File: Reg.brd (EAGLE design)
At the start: 30.5 x 21 mm, 28 parts, among them Q1 NPN2SC3422-2, Q2 NPN2SC3325, Q3 PNP2SA1313, Q4 NPN2SC3325, Q5 NPN2SC3422-2, Q6 NPN2SC3325, Q7 PNP2SA1313, Q8 PNP2SA1313

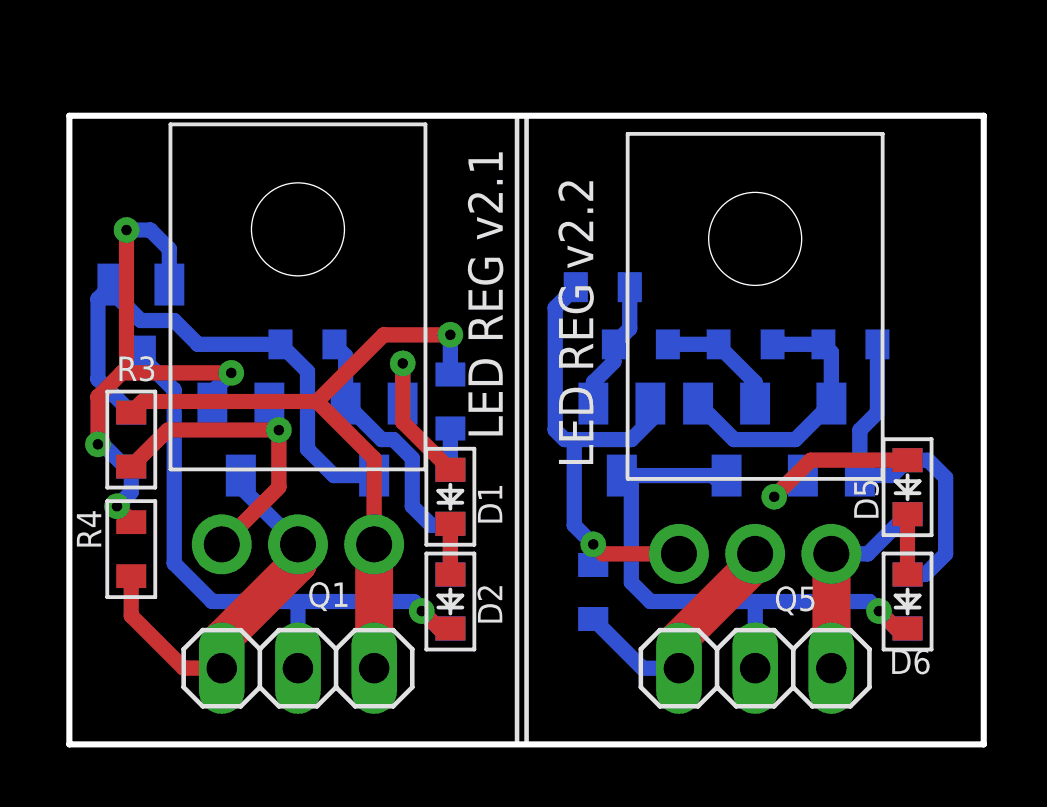
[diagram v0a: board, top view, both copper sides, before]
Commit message: 幅を小さくした
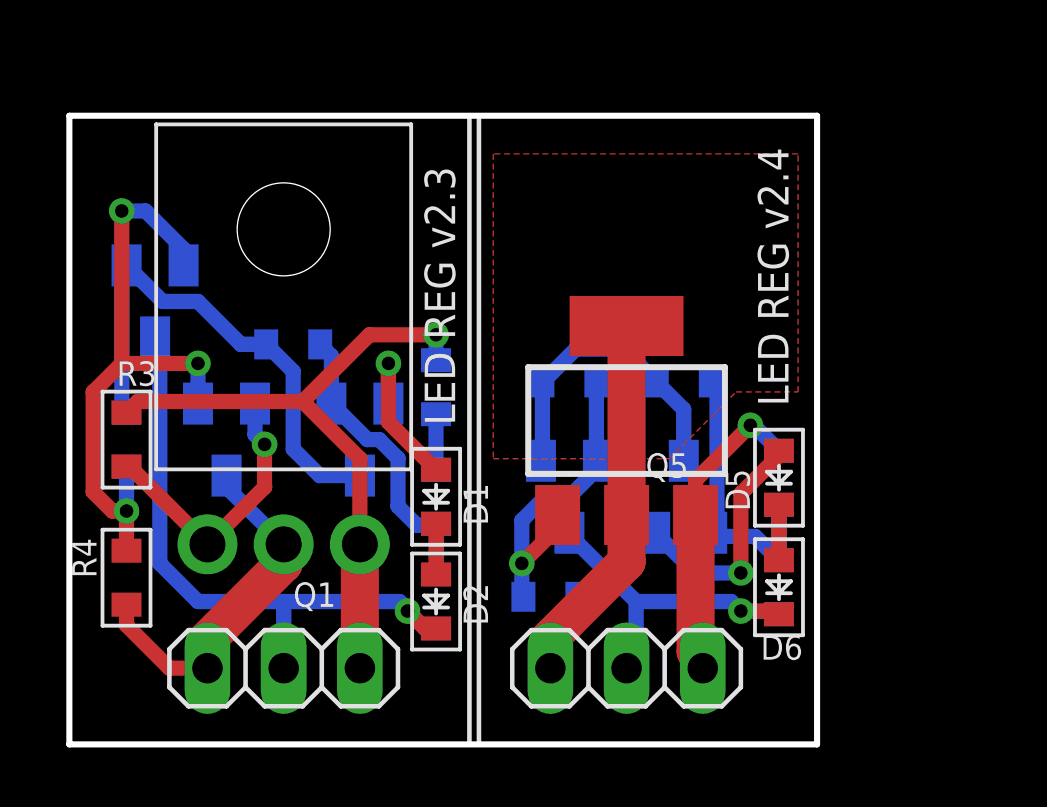
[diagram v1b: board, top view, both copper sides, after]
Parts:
- removed D3, D4: BLUE, my_rcl:D1608
- removed Q7: PNP2SA1313, my_ic:SC59
- D1, D2: value SHORT -> BLUE
- Q1: value NPN2SC3422-2 -> NPN
- Q2, Q4, Q6: value NPN2SC3325 -> NPN
- Q3, Q8: value PNP2SA1313 -> PNP
- Q5: value NPN2SC3422-2 -> NPN; device my_ic:TO126-2 -> my_ic:SOT223
- R10: value 0.75k -> 1.5k
- moved R6 11.5 mm to (12.2, 8.26), turned to 90 degrees
- moved R7 6.97 mm to (12.2, 11.9), turned to 90 degrees
- moved Q5 6.17 mm to (18.6, 10.8)
- moved C1 5.70 mm to (20.5, 12.1)
- moved Q6 5.28 mm to (20.5, 8.26)
- moved D6 4.31 mm to (23.7, 5.24)
- moved R5 4.31 mm to (23.7, 5.24)
- moved D5 4.30 mm to (23.7, 8.89)
- moved R12 4.30 mm to (23.7, 8.89), turned to 90 degrees
- moved JP2 4.29 mm to (18.6, 2.54)
- moved R10 3.36 mm to (16.7, 12.1), turned to 180 degrees
- moved Q8 2.58 mm to (16.7, 8.26)
- moved R9 1.44 mm to (16.0, 4.92), turned to 180 degrees
- moved R4 0.97 mm to (1.91, 5.56)
- moved Q3 0.79 mm to (2.86, 14.8)
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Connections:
- removed net N$11: Q7.2, R6.2, R7.1
- removed net N$15: Q8.1, R10.1, R7.2
- net GND1: no longer Q7.3
- net IN1: now also Q5.4
- net N$12: now also Q8.1, R10.1; no longer Q7.1, R6.1
- net N$16: now also Q5.1; no longer Q5.3
- net N$3: now also R6.1; no longer D3.K
- net N$5: now also R6.2, R7.1; no longer D3.A, D4.K
- net OUT: now also R7.2; no longer D4.A
- net OUT1: now also Q5.3; no longer Q5.1
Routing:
- net GND1: track 20.6 -> 11.8 mm
- net IN1: track 8.40 -> 15.2 mm
- net N$16: track 16.6 -> 10.8 mm
- net N$15: track 4.38 -> 0.00 mm
- net N$11: track 4.17 -> 0.00 mm
- net OUT1: track 6.90 -> 10.3 mm, vias 0 -> 1
- net N$13: track 12.0 -> 9.62 mm
- net N$1: track 19.1 -> 21.0 mm, vias 4 -> 3
- net N$9: track 6.20 -> 8.01 mm
- net N$6: track 11.0 -> 9.39 mm
- net N$12: track 9.21 -> 10.3 mm
- net IN: track 13.3 -> 12.2 mm
- net OUT: track 22.7 -> 21.9 mm
- net N$10: track 18.0 -> 17.2 mm
- added copper zone on layer 1, net IN1
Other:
- board size 30.5 x 21 mm -> 24.9 x 21 mm
- board text added: "LED REG v2.3"
- board text added: "LED REG v2.4"
- board text removed: "LED REG v2.1"
- board text removed: "LED REG v2.2"

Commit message: V-CUT
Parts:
- added C10, C11, C12, C13, C14, C15, C16, C17, C18, C2, C3, C4, C5, C6, C8, C9: 100p, my_rcl:1608
- added D10, D11, D12, D13, D14, D15, D16, D17, D18, D19, D20, D21, D22, D23, D24, D25, D26, D27, D28, D29, D3, D30, D31, D32, D33, D34, D35, D36, D4, D7, D8, D9: BLUE, my_rcl:D1608
- added JP10, JP11, JP12, JP13, JP14, JP15, JP16, JP17, JP18, JP3, JP4, JP5, JP6, JP7, JP8, JP9: CON, pinhead:1X03
- added Q10, Q14, Q17, Q21, Q24, Q28, Q31, Q35, Q38, Q42, Q45, Q49, Q52, Q56, Q59, Q63: PNP, my_ic:SC59
- added Q11, Q13, Q16, Q18, Q20, Q23, Q25, Q27, Q30, Q32, Q34, Q37, Q39, Q41, Q44, Q46, Q48, Q51, Q53, Q55, Q58, Q60, Q62, Q9: NPN, my_ic:SC59
- added Q12, Q19, Q26, Q33, Q40, Q47, Q54, Q61: NPN, my_ic:SOT223
- added Q15, Q22, Q29, Q36, Q43, Q50, Q57, Q7: NPN, my_ic:TO126-2
- added R11, R13, R15, R16, R17, R18, R19, R20, R21, R22, R23, R25, R26, R27, R28, R29, R30, R31, R32, R33, R35, R36, R37, R38, R39, R40, R41, R42, R43, R45, R46, R47, R48, R49, R50, R51, R52, R53, R55, R56, R57, R58, R59, R60, R61, R62, R63, R65, R66, R67, R68, R69, R70, R71, R72, R73, R75, R76, R77, R78, R79, R8, R80, R81, R82, R83, R85, R86, R87, R88, R89, R90: 1.5k, my_rcl:1608
- added R14, R24, R34, R44, R54, R64, R74, R84: 10k, my_rcl:1608
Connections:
- new net GND10: D22.K, JP11.2, Q38.3, R51.1
- new net GND11: D24.K, JP12.2, Q42.3, R55.1
- new net GND12: D26.K, JP13.2, Q45.3, R61.1
- new net GND13: D28.K, JP14.2, Q49.3, R65.1
- new net GND14: D30.K, JP15.2, Q52.3, R71.1
- new net GND15: D32.K, JP16.2, Q56.3, R75.1
- new net GND16: D34.K, JP17.2, Q59.3, R81.1
- new net GND17: D36.K, JP18.2, Q63.3, R85.1
- new net GND2: D4.K, JP3.2, Q10.3, R8.1
- new net GND3: D8.K, JP4.2, Q14.3, R15.1
- new net GND4: D10.K, JP5.2, Q17.3, R21.1
- new net GND5: D12.K, JP6.2, Q21.3, R25.1
- new net GND6: D14.K, JP7.2, Q24.3, R31.1
- new net GND7: D16.K, JP8.2, Q28.3, R35.1
- new net GND8: D18.K, JP9.2, Q31.3, R41.1
- new net GND9: D20.K, JP10.2, Q35.3, R45.1
- new net IN10: JP11.1, Q36.2, Q39.3, R53.2
- new net IN11: JP12.1, Q40.2, Q40.4, R56.2
- new net IN12: JP13.1, Q43.2, Q46.3, R63.2
- new net IN13: JP14.1, Q47.2, Q47.4, R66.2
- new net IN14: JP15.1, Q50.2, Q53.3, R73.2
- new net IN15: JP16.1, Q54.2, Q54.4, R76.2
- new net IN16: JP17.1, Q57.2, Q60.3, R83.2
- new net IN17: JP18.1, Q61.2, Q61.4, R86.2
- new net IN2: JP3.1, Q11.3, Q7.2, R13.2
- new net IN3: JP4.1, Q12.2, Q12.4, R16.2
- new net IN4: JP5.1, Q15.2, Q18.3, R23.2
- new net IN5: JP6.1, Q19.2, Q19.4, R26.2
- new net IN6: JP7.1, Q22.2, Q25.3, R33.2
- new net IN7: JP8.1, Q26.2, Q26.4, R36.2
- new net IN8: JP9.1, Q29.2, Q32.3, R43.2
- new net IN9: JP10.1, Q33.2, Q33.4, R46.2
- new net N$100: Q59.2, Q60.1, R82.2, R83.1
- new net N$101: C17.1, Q58.3, Q59.1, R82.1
- new net N$102: Q57.3, Q60.2, R84.2
- new net N$103: D35.K, D36.A
- new net N$104: D35.A, Q62.2
- new net N$105: C18.1, Q62.3, Q63.1, R87.1
- new net N$106: Q61.1, Q63.2, R86.1, R87.2
- new net N$107: C18.2, Q62.1, R85.2, R88.1
- new net N$108: R89.2, R90.1
- new net N$11: D3.K, D4.A
- new net N$14: D3.A, Q9.2
- new net N$15: Q10.2, Q11.1, R11.2, R13.1
- new net N$17: C2.1, Q10.1, Q9.3, R11.1
- new net N$18: Q11.2, Q7.3, R14.2
- new net N$19: D7.K, D8.A
- new net N$20: D7.A, Q13.2
- new net N$21: C3.1, Q13.3, Q14.1, R17.1
- new net N$22: Q12.1, Q14.2, R16.1, R17.2
- new net N$23: C3.2, Q13.1, R15.2, R18.1
- new net N$24: R19.2, R20.1
- new net N$25: C4.2, Q16.1, R21.2, R29.1
- new net N$26: D10.A, D9.K
- new net N$27: D9.A, Q16.2
- new net N$28: Q17.2, Q18.1, R22.2, R23.1
- new net N$29: C4.1, Q16.3, Q17.1, R22.1
- new net N$30: Q15.3, Q18.2, R24.2
- new net N$31: D11.K, D12.A
- new net N$32: D11.A, Q20.2
- new net N$33: C5.1, Q20.3, Q21.1, R27.1
- new net N$34: Q19.1, Q21.2, R26.1, R27.2
- new net N$35: C5.2, Q20.1, R25.2, R28.1
- new net N$36: R29.2, R30.1
- new net N$37: C6.2, Q23.1, R31.2, R39.1
- new net N$38: D13.K, D14.A
- new net N$39: D13.A, Q23.2
- new net N$40: Q24.2, Q25.1, R32.2, R33.1
- new net N$41: C6.1, Q23.3, Q24.1, R32.1
- new net N$42: Q22.3, Q25.2, R34.2
- new net N$43: D15.K, D16.A
- new net N$44: D15.A, Q27.2
- new net N$45: C8.1, Q27.3, Q28.1, R37.1
- new net N$46: Q26.1, Q28.2, R36.1, R37.2
- new net N$47: C8.2, Q27.1, R35.2, R38.1
- new net N$48: R39.2, R40.1
- new net N$49: C9.2, Q30.1, R41.2, R49.1
- new net N$50: D17.K, D18.A
- new net N$51: D17.A, Q30.2
- new net N$52: Q31.2, Q32.1, R42.2, R43.1
- new net N$53: C9.1, Q30.3, Q31.1, R42.1
- new net N$54: Q29.3, Q32.2, R44.2
- new net N$55: D19.K, D20.A
- new net N$56: D19.A, Q34.2
- new net N$57: C10.1, Q34.3, Q35.1, R47.1
- new net N$58: Q33.1, Q35.2, R46.1, R47.2
- new net N$59: C10.2, Q34.1, R45.2, R48.1
- new net N$60: R49.2, R50.1
- new net N$61: C11.2, Q37.1, R51.2, R59.1
- new net N$62: D21.K, D22.A
- new net N$63: D21.A, Q37.2
- new net N$64: Q38.2, Q39.1, R52.2, R53.1
- new net N$65: C11.1, Q37.3, Q38.1, R52.1
- new net N$66: Q36.3, Q39.2, R54.2
- new net N$67: D23.K, D24.A
- new net N$68: D23.A, Q41.2
- new net N$69: C12.1, Q41.3, Q42.1, R57.1
- new net N$7: C2.2, Q9.1, R19.1, R8.2
- new net N$70: Q40.1, Q42.2, R56.1, R57.2
- new net N$71: C12.2, Q41.1, R55.2, R58.1
- new net N$72: R59.2, R60.1
- new net N$73: C13.2, Q44.1, R61.2, R69.1
- new net N$74: D25.K, D26.A
- new net N$75: D25.A, Q44.2
- new net N$76: Q45.2, Q46.1, R62.2, R63.1
- new net N$77: C13.1, Q44.3, Q45.1, R62.1
- new net N$78: Q43.3, Q46.2, R64.2
- new net N$79: D27.K, D28.A
- new net N$80: D27.A, Q48.2
- new net N$81: C14.1, Q48.3, Q49.1, R67.1
- new net N$82: Q47.1, Q49.2, R66.1, R67.2
- new net N$83: C14.2, Q48.1, R65.2, R68.1
- new net N$84: R69.2, R70.1
- new net N$85: C15.2, Q51.1, R71.2, R79.1
- new net N$86: D29.K, D30.A
- new net N$87: D29.A, Q51.2
- new net N$88: Q52.2, Q53.1, R72.2, R73.1
- new net N$89: C15.1, Q51.3, Q52.1, R72.1
- new net N$90: Q50.3, Q53.2, R74.2
- new net N$91: D31.K, D32.A
- new net N$92: D31.A, Q55.2
- new net N$93: C16.1, Q55.3, Q56.1, R77.1
- new net N$94: Q54.1, Q56.2, R76.1, R77.2
- new net N$95: C16.2, Q55.1, R75.2, R78.1
- new net N$96: R79.2, R80.1
- new net N$97: C17.2, Q58.1, R81.2, R89.1
- new net N$98: D33.K, D34.A
- new net N$99: D33.A, Q58.2
- new net OUT10: JP11.3, Q36.1, R54.1, R60.2
- new net OUT11: JP12.3, Q40.3, R58.2
- new net OUT12: JP13.3, Q43.1, R64.1, R70.2
- new net OUT13: JP14.3, Q47.3, R68.2
- new net OUT14: JP15.3, Q50.1, R74.1, R80.2
- new net OUT15: JP16.3, Q54.3, R78.2
- new net OUT16: JP17.3, Q57.1, R84.1, R90.2
- new net OUT17: JP18.3, Q61.3, R88.2
- new net OUT2: JP3.3, Q7.1, R14.1, R20.2
- new net OUT3: JP4.3, Q12.3, R18.2
- new net OUT4: JP5.3, Q15.1, R24.1, R30.2
- new net OUT5: JP6.3, Q19.3, R28.2
- new net OUT6: JP7.3, Q22.1, R34.1, R40.2
- new net OUT7: JP8.3, Q26.3, R38.2
- new net OUT8: JP9.3, Q29.1, R44.1, R50.2
- new net OUT9: JP10.3, Q33.3, R48.2
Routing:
- net OUT8: track 0.00 -> 21.9 mm, vias 0 -> 1
- net OUT6: track 0.00 -> 21.9 mm, vias 0 -> 1
- net OUT10: track 0.00 -> 21.9 mm, vias 0 -> 1
- net OUT4: track 0.00 -> 21.9 mm, vias 0 -> 1
- net OUT2: track 0.00 -> 21.9 mm, vias 0 -> 1
- net OUT14: track 0.00 -> 21.9 mm, vias 0 -> 1
- net OUT12: track 0.00 -> 21.9 mm, vias 0 -> 1
- net OUT16: track 0.00 -> 21.9 mm, vias 0 -> 1
- net GND8: track 0.00 -> 21.2 mm, vias 0 -> 1
- net GND2: track 0.00 -> 21.2 mm, vias 0 -> 1
- net GND14: track 0.00 -> 21.2 mm, vias 0 -> 1
- net GND4: track 0.00 -> 21.2 mm, vias 0 -> 1
- net GND10: track 0.00 -> 21.2 mm, vias 0 -> 1
- net GND6: track 0.00 -> 21.2 mm, vias 0 -> 1
- net GND16: track 0.00 -> 21.2 mm, vias 0 -> 1
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- added copper zone on layer 1, net IN11
- added copper zone on layer 1, net IN13
- added copper zone on layer 1, net IN15
- added copper zone on layer 1, net IN17
- added copper zone on layer 1, net IN3
- added copper zone on layer 1, net IN5
- added copper zone on layer 1, net IN7
- added copper zone on layer 1, net IN9
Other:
- board size 24.9 x 21 mm -> 78.4 x 65.7 mm
- board text added: "<- V-CUT"
